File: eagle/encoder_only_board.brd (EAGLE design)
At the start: 34.5 x 29.1 mm, 30 parts, among them IC2 AT42QT1010SOT23, J1 FH12-6S-0.5SH(55), J2 FH12-6S-0.5SH(55)

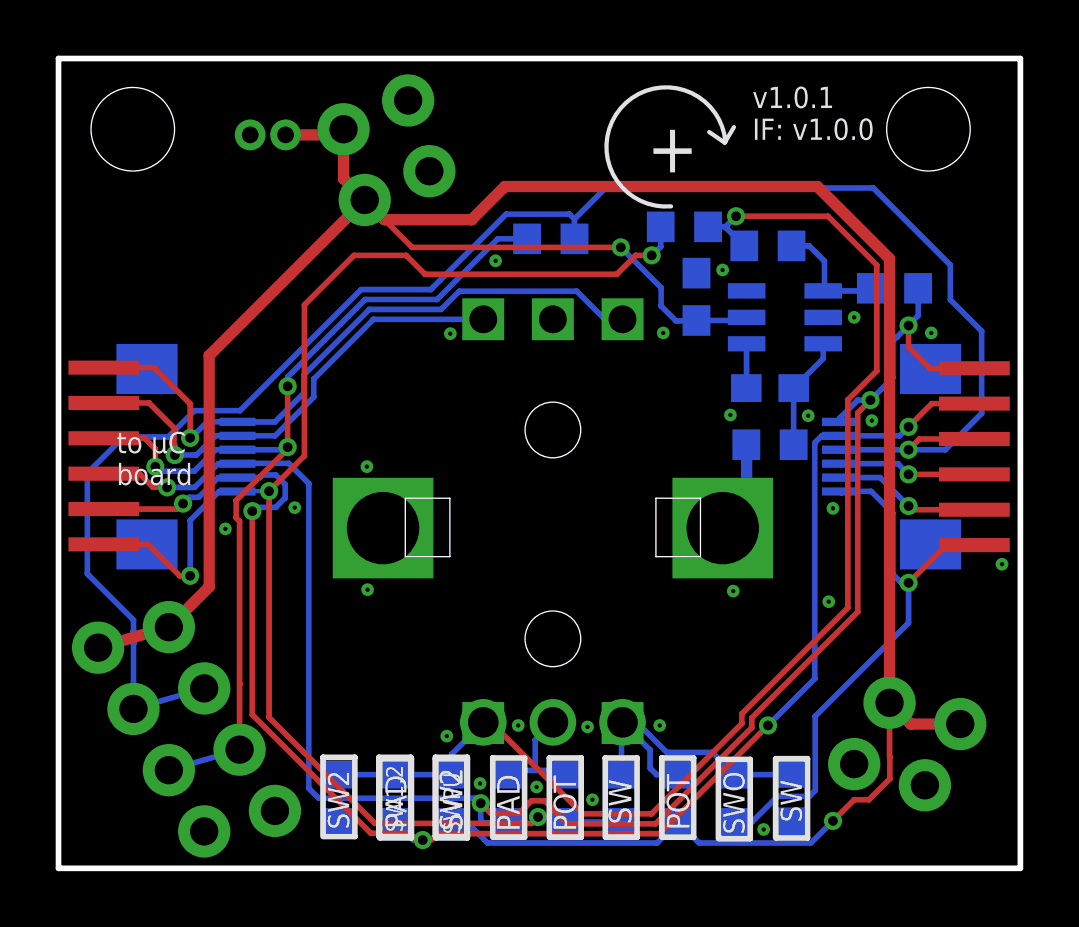
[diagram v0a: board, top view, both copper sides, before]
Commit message: Add second power connector for chaining encoder boards
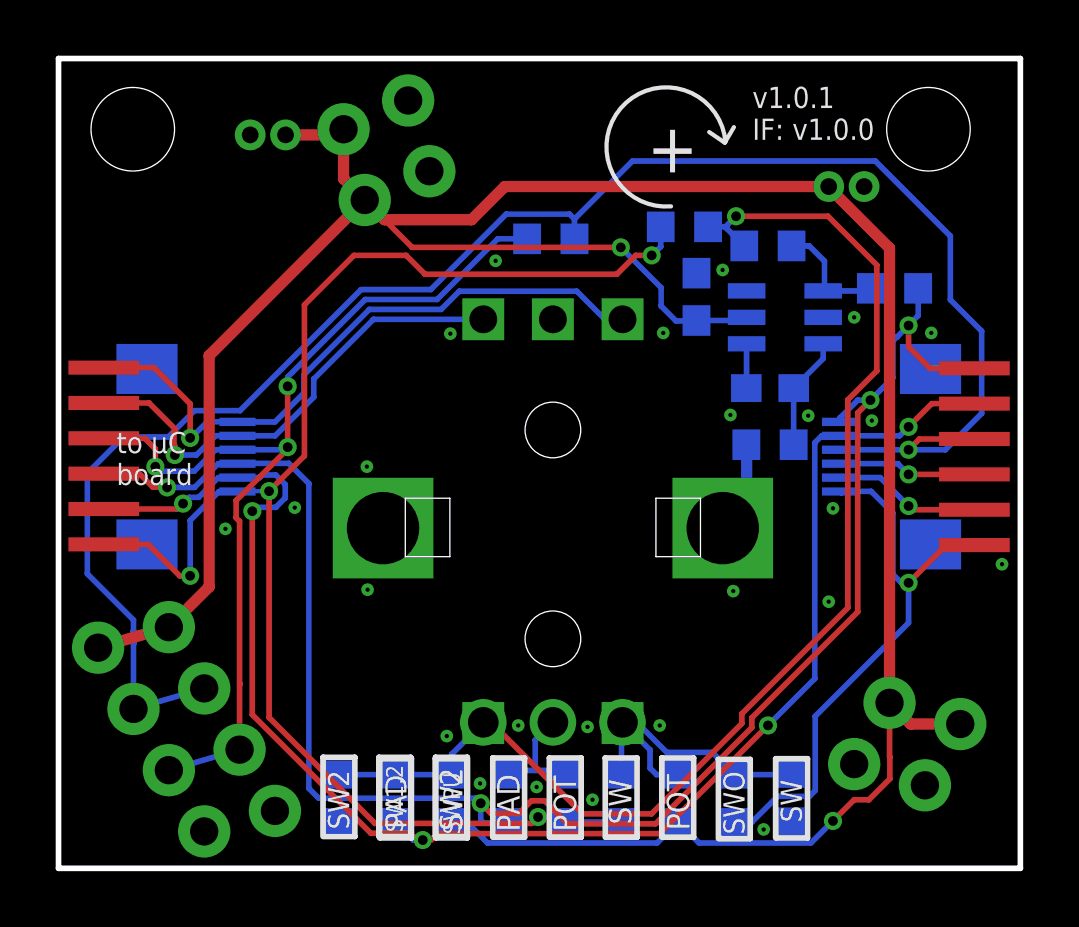
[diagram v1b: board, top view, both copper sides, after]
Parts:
- added POWER1: 2PIN_1.27MM, edge:1X02_1.27MM_NO_SILK
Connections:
- net GND: now also POWER1.10
- net VCC: now also POWER1.9
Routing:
- net LED_OUT: track 63.0 -> 64.4 mm
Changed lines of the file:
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@@
 <attribute name="VALUE" x="28.1178" y="3.175" size="1.27" layer="28" rot="MR270"/>
+</element>
+<element name="POWER1" library="edge" package="1X02_1.27MM_NO_SILK" value="2PIN_1.27MM" x="27.5336" y="24.4856" smashed="yes">
+<attribute name="VALUE" x="26.2636" y="21.3106" size="1.27" layer="27"/>
 </element>
 </elements>
@@
 <wire x1="5.2832" y1="18.415" x2="5.2832" y2="10.1092" width="0.4064" layer="1"/>
 <wire x1="5.2832" y1="18.415" x2="10.8712" y2="24.003" width="0.4064" layer="1"/>
-<wire x1="29.718" y1="5.9436" x2="29.718" y2="21.8948" width="0.4064" layer="1"/>
-<wire x1="29.718" y1="21.8948" x2="27.1272" y2="24.4856" width="0.4064" layer="1"/>
-<wire x1="27.1272" y1="24.4856" x2="15.9004" y2="24.4856" width="0.4064" layer="1"/>
+<wire x1="29.718" y1="5.9436" x2="29.718" y2="22.2758" width="0.4064" layer="1"/>
+<wire x1="29.718" y1="22.2758" x2="27.5082" y2="24.4856" width="0.4064" layer="1"/>
+<wire x1="27.5082" y1="24.4856" x2="15.9004" y2="24.4856" width="0.4064" layer="1"/>
 <wire x1="15.9004" y1="24.4856" x2="14.7066" y2="23.2918" width="0.4064" layer="1"/>
 <wire x1="14.7066" y1="23.2918" x2="11.5824" y2="23.2918" width="0.4064" layer="1"/>
@@
 <wire x1="10.1092" y1="26.543" x2="9.906" y2="26.3398" width="0.4064" layer="1"/>
 <wire x1="9.906" y1="26.3398" x2="8.0264" y2="26.3398" width="0.4064" layer="1"/>
+<contactref element="POWER1" pad="9"/>
+<wire x1="27.5336" y1="24.4856" x2="27.5082" y2="24.4856" width="0.4064" layer="1"/>
 </signal>
 <signal name="GND">
@@
 <via x="27.5336" y="9.5758" extent="1-16" drill="0.1524"/>
 <via x="19.05" y="2.4638" extent="1-16" drill="0.1524"/>
-<contactref element="R2" pad="2"/>
 <contactref element="R4" pad="2"/>
 <via x="25.1968" y="1.397" extent="1-16" drill="0.1524"/>
@@
 <via x="16.383" y="5.1308" extent="1-16" drill="0.1524"/>
 <via x="15.0114" y="3.048" extent="1-16" drill="0.1524"/>
+<contactref element="POWER1" pad="10"/>
 </signal>
 <signal name="ENC1B">
@@
 <contactref element="R21" pad="1"/>
 <wire x1="2.565403125" y1="5.72509375" x2="5.105403125" y2="6.46169375" width="0.2032" layer="16"/>
-<wire x1="19.519" y1="24.4348" x2="18.4014" y2="23.3172" width="0.2032" layer="16"/>
-<wire x1="29.1324125" y1="24.4348" x2="19.519" y2="24.4348" width="0.2032" layer="16"/>
+<wire x1="20.4842" y1="25.4" x2="18.4014" y2="23.3172" width="0.2032" layer="16"/>
+<wire x1="29.2086125" y1="25.4" x2="20.4842" y2="25.4" width="0.2032" layer="16"/>
 <wire x1="2.565403125" y1="5.72509375" x2="2.565403125" y2="8.05200625" width="0.2032" layer="16"/>
 <wire x1="2.565403125" y1="8.05200625" x2="2.576509375" y2="8.09345625" width="0.2032" layer="16"/>
@@
 <contactref element="J2" pad="3"/>
 <wire x1="0.9078" y1="14.192" x2="0.9078" y2="10.5767875" width="0.2032" layer="16"/>
-<wire x1="31.90170625" y1="21.66550625" x2="29.1324125" y2="24.4348" width="0.2032" layer="16"/>
+<wire x1="31.90170625" y1="22.70690625" x2="29.2086125" y2="25.4" width="0.2032" layer="16"/>
 <wire x1="0.9078" y1="10.5767875" x2="2.565403125" y2="8.919184375" width="0.2032" layer="16"/>
 <wire x1="2.565403125" y1="8.534215625" x2="2.565403125" y2="8.919184375" width="0.2032" layer="16"/>
-<wire x1="31.90170625" y1="21.66550625" x2="31.90170625" y2="20.41850625" width="0.2032" layer="16"/>
+<wire x1="31.90170625" y1="22.70690625" x2="31.90170625" y2="20.41850625" width="0.2032" layer="16"/>
 <wire x1="31.90170625" y1="20.41850625" x2="33.0266" y2="19.2936125" width="0.2032" layer="16"/>
 <wire x1="33.0266" y1="16.3388" x2="33.0266" y2="19.2936125" width="0.2032" layer="16"/>

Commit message: Fix encoder only board issues for manufacturing;
The board was a couple of mils too wide to get 3x3 boards on a panel.
Thus the components were moved a bit to the left and traces squeezed to
fit in a smaller space.

Also there were some duplicate texts in the jumper "legends" below the
encoder and those texts were removed.

The hole on the right top corner was moved to a symmetrical position
compared to the one on the left top.
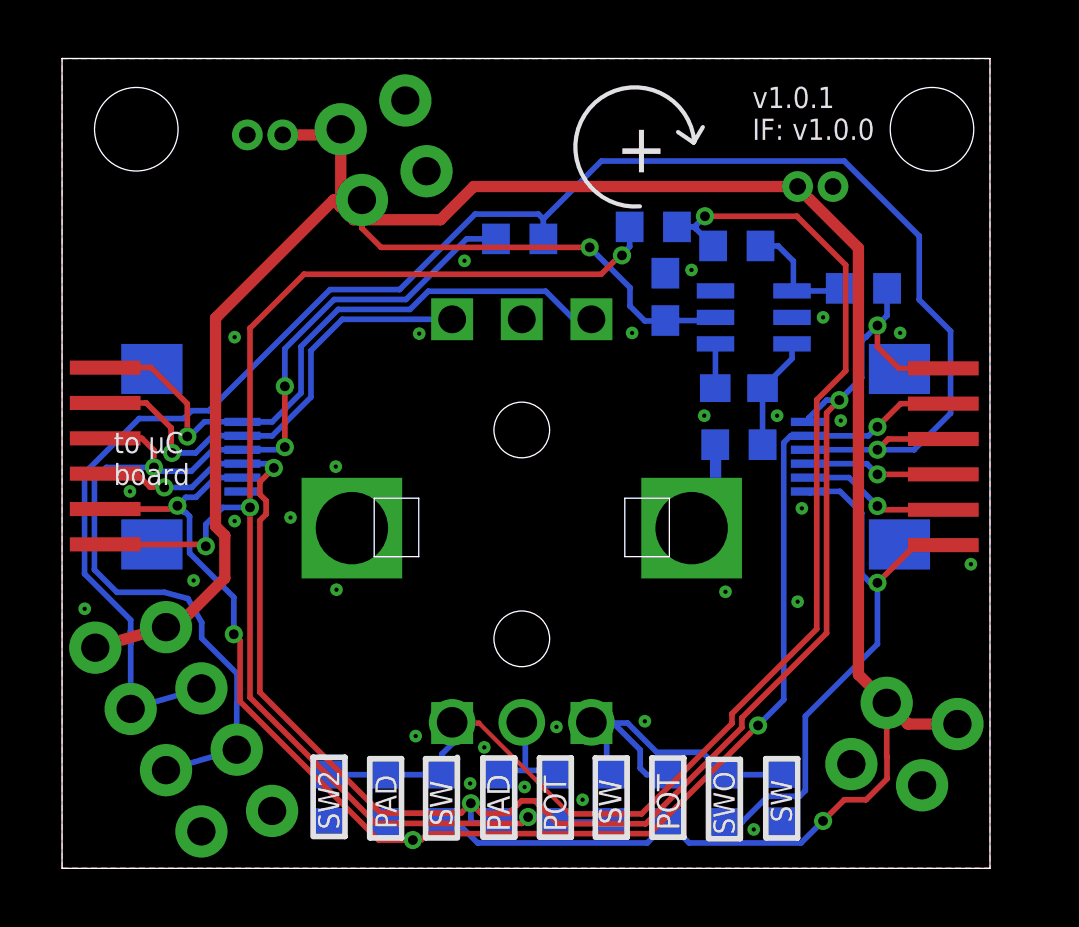
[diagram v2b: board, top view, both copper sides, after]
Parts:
- moved J2 1.12 mm to (26.8, 14.8)
- moved R38 1.12 mm to (28.8, 20.8)
- moved C16 1.12 mm to (24.3, 17.2)
- moved C17 1.12 mm to (21.7, 20.5)
- moved ENC1 1.12 mm to (16.5, 12.2)
- moved IC2 1.12 mm to (24.8, 19.8)
- moved POWER1 1.12 mm to (26.4, 24.5)
- moved R16 1.12 mm to (24.3, 15.2)
- moved R21 1.12 mm to (16.4, 22.6)
- moved R24 1.12 mm to (24.2, 22.4)
- moved R25 1.12 mm to (16.5, 12.2)
- moved R6 1.12 mm to (21.2, 23.0)
- moved U$1 1.12 mm to (31.6, 18.0)
- moved R4 0.36 mm to (25.9, 2.54)
- moved R1 0.36 mm to (13.6, 2.51)
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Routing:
- net LED_IN: track 35.3 -> 38.5 mm
- net ENC2B: track 56.9 -> 53.9 mm
- net SW_IN: track 53.5 -> 51.0 mm
- net VCC: track 102.0 -> 103.5 mm
- net ENC2A: track 62.3 -> 61.1 mm, vias 4 -> 5
- net LED_OUT: track 64.4 -> 63.4 mm
- net ENC_SW: track 8.68 -> 9.49 mm
- net POT+: track 3.16 -> 3.92 mm
- net ENC1B: track 17.4 -> 16.7 mm
- net ENC1A: track 23.4 -> 22.7 mm
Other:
- board size 34.5 x 29.1 mm -> 33.3 x 29.1 mm
- board text removed: "SW1,2"
- board text removed: "SWPU"
